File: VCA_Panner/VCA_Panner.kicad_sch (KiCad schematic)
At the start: 40 parts, among them J1 CV1, J2 Ch1_in, J3 Ch1_out, J4 CV2, J5 Ch2_in, J6 Ch2_out, SW1 SW_DPDT_x2, SW2 SW_DPDT_x2, U1 TL074, U2 AS3360, U3 TL072

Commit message: feitw bugfixes
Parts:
- removed C5: 47pF, symbol Device:C
- removed SW1, SW2: SW_DPDT_x2, symbol Switch:SW_DPDT_x2
- removed U3: TL072, 4ms_Package_SSOP:TSSOP-8_4.4x3mm_Pitch0.65mm, symbol PCM_4ms_IC:TL072
- added C10, C4, C8, C9: 0.1uF, Capacitor_SMD:C_0805_2012Metric_Pad1.18x1.45mm_HandSolder, symbol Device:C
- added C11: 470p, Capacitor_SMD:C_0805_2012Metric_Pad1.18x1.45mm_HandSolder, symbol Device:C
- added C12, C13: 47u, Capacitor_THT:CP_Radial_D4.0mm_P2.00mm, symbol Device:C_Polarized
- added D3, D4: 1N5819, Diode_THT:D_DO-41_SOD81_P2.54mm_Vertical_AnodeUp, symbol Diode:1N5819
- added J5: ~, mort_mix:Pins_2x05_2.54mm_TH_Europower_shrouded, symbol Connector_Generic:Conn_02x05_Odd_Even
- added R19, R21, R23, R7: 10k, Resistor_SMD:R_0805_2012Metric_Pad1.20x1.40mm_HandSolder, symbol Device:R
- added R20, R32, R36: 100k, Resistor_SMD:R_0805_2012Metric_Pad1.20x1.40mm_HandSolder, symbol Device:R
- added R22, R24, R8: 56k, Resistor_SMD:R_0805_2012Metric_Pad1.20x1.40mm_HandSolder, symbol Device:R
- added R25: 20k, Resistor_SMD:R_0805_2012Metric_Pad1.20x1.40mm_HandSolder, symbol Device:R
- added R26, R27: 47k, Resistor_SMD:R_0805_2012Metric_Pad1.20x1.40mm_HandSolder, symbol Device:R
- added R28: 330k, Resistor_SMD:R_0805_2012Metric_Pad1.20x1.40mm_HandSolder, symbol Device:R
- added R29, R33, R35: 51k, Resistor_SMD:R_0805_2012Metric_Pad1.20x1.40mm_HandSolder, symbol Device:R
- added R34: 1k, Resistor_SMD:R_0805_2012Metric_Pad1.20x1.40mm_HandSolder, symbol Device:R
- added R37, R38: 10, Resistor_SMD:R_0805_2012Metric_Pad1.20x1.40mm_HandSolder, symbol Device:R
- added R39, R40: 400k, Resistor_SMD:R_0805_2012Metric_Pad1.20x1.40mm_HandSolder, symbol Device:R
- added RV3, RV4: 100k_B, mort_mix:Potentiometer_Alpha_RD901F-40-00D_Single_Vertical_withhole, symbol Device:R_Potentiometer
- added U2, U3: TL074, Package_SO:SO-14_3.9x8.65mm_P1.27mm, symbol Amplifier_Operational:TL074
- C1, C2: value 47pF -> 0.1uF; footprint (none) -> Capacitor_SMD:C_0805_2012Metric_Pad1.18x1.45mm_HandSolder
- C3, C7: value 22pF -> 0.1uF; footprint (none) -> Capacitor_SMD:C_0805_2012Metric_Pad1.18x1.45mm_HandSolder
- C5: renamed from C4; value 10nF -> 4.7n; footprint (none) -> Capacitor_SMD:C_0805_2012Metric_Pad1.18x1.45mm_HandSolder
- C6: value 47pF -> 470p; footprint (none) -> Capacitor_SMD:C_0805_2012Metric_Pad1.18x1.45mm_HandSolder
- D1, D2: footprint (none) -> Diode_SMD:D_0805_2012Metric_Pad1.15x1.40mm_HandSolder
- J1: footprint (none) -> mort_mix:PJ398SM
- J2: renamed from J4; footprint (none) -> mort_mix:PJ398SM
- J3: renamed from J2; footprint (none) -> mort_mix:Jack_3.5mm_QingPu_WQP-PJ366ST_Vertical
- J4: renamed from J3; footprint (none) -> mort_mix:Jack_3.5mm_QingPu_WQP-PJ366ST_Vertical
- J6: renamed from J5; footprint (none) -> mort_mix:PJ398SM
- J7: renamed from J6; footprint (none) -> mort_mix:PJ398SM
- R1, R11, R2: footprint (none) -> Resistor_SMD:R_0805_2012Metric_Pad1.20x1.40mm_HandSolder
- R10, R18: value 100k -> 56k; footprint (none) -> Resistor_SMD:R_0805_2012Metric_Pad1.20x1.40mm_HandSolder
- R12: value 12k -> 47k; footprint (none) -> Resistor_SMD:R_0805_2012Metric_Pad1.20x1.40mm_HandSolder
- R13: value 100k -> 47k; footprint (none) -> Resistor_SMD:R_0805_2012Metric_Pad1.20x1.40mm_HandSolder
- R14: value 47k -> 330k; footprint (none) -> Resistor_SMD:R_0805_2012Metric_Pad1.20x1.40mm_HandSolder
- R15: value 1k -> 100k; footprint (none) -> Resistor_SMD:R_0805_2012Metric_Pad1.20x1.40mm_HandSolder
- R16, R6: value 47k -> 100k; footprint (none) -> Resistor_SMD:R_0805_2012Metric_Pad1.20x1.40mm_HandSolder
- R17, R5, R9: value 100k -> 10k; footprint (none) -> Resistor_SMD:R_0805_2012Metric_Pad1.20x1.40mm_HandSolder
- R3: value 20k -> 10k; footprint (none) -> Resistor_SMD:R_0805_2012Metric_Pad1.20x1.40mm_HandSolder
- R30: renamed from R7; footprint (none) -> Resistor_SMD:R_0805_2012Metric_Pad1.20x1.40mm_HandSolder
- R31: renamed from R8; value 47k -> 51k; footprint (none) -> Resistor_SMD:R_0805_2012Metric_Pad1.20x1.40mm_HandSolder
- R4: value 12k -> 56k; footprint (none) -> Resistor_SMD:R_0805_2012Metric_Pad1.20x1.40mm_HandSolder
- RV1, RV2: value 10k -> 100k_B; footprint (none) -> mort_mix:Potentiometer_Alpha_RD901F-40-00D_Single_Vertical_withhole
- U1: footprint (none) -> Package_SO:SO-14_3.9x8.65mm_P1.27mm
- U5: renamed from U2; footprint (none) -> Package_SO:SOIC-16_3.9x9.9mm_P1.27mm
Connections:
- net CV_to_ch1 is gone; now on net CV2: J2.T
- net CV_to_ch2 is gone; now on an unnamed net: D2.2 (A)
- net audio_to_ch1 is gone; now on net audio_from_ch2: J7.TN
- net +12V: now also C1.1, C2.1, C3.1, U1.4 (V+), C13.1, C4.2, R37.1, R39.2, R40.2, U2.4 (V+), U3.4 (V+)
- net -12V: now also C7.2, U1.11 (V-), C10.2, C12.2, C8.2, C9.2, R38.2, U2.11 (V-), U3.11 (V-); no longer R12.1, R4.1
- net GND: now also C1.2, C2.2, C3.2, C7.1, R13.2, C10.1, C12.1, C13.2, C4.1, C8.1, C9.1, J5.3 (Pin_3), J5.4 (Pin_4), J5.5 (Pin_5), J5.6 (Pin_6), J5.7 (Pin_7), J5.8 (Pin_8), R27.2, R35.1, RV3.1, RV4.1, U2.10 (+), U2.3 (+), U3.12 (+), U3.5 (+); no longer R16.1, U1.10 (+), U1.3 (+)
- net at R31.2, U5.2 (IO1): now also U2.6 (-); no longer C3.1, R5.1
- net CV1: now reaches D1.1 (K)
- net CV1: now also R12.1, R6.2, RV1.3
- net at R12.2: now also R13.1, RV1.2, U1.3 (+); no longer RV2.3
- net at R18.2: now also R23.1, U3.13 (-)
- net at R14.1: now also RV2.3; no longer J6.T
- net at R6.1: now also R1.2, U1.2 (-); no longer J3.R
- net audio1_to_vca1: now reaches U5.6 (II1)
- net audio1_to_vca1: now also R29.2; no longer R6.2
- net at R11.2: now also R5.1, U2.1; no longer U5.10 (VC2)
- net at R9.1: now also R4.2, U1.13 (-); no longer U1.14
- net at R3.2: now also U1.9 (-), R8.1; no longer U5.5 (VC1)
- net at R17.2: now also R22.1, U3.9 (-)
- net at R15.2: now also R20.1, U3.2 (-); no longer J7.T
- net at R14.2: now also R40.1; no longer U5.9 (II2)
- net CV_from_ch1: no longer names the net of J2.TN
- net CV_from_ch2 renamed CV2
- net CV2: now also R20.2, R26.1, RV3.3
- new net: R3.1, R9.2, U1.8
- new net: RV2.2, U1.10 (+)
- new net: R15.1, R21.2, U3.1
- new net: R26.2, R27.1, RV3.2, U3.3 (+)
- new net: R18.1, R24.2, U3.14
- new net: R10.1, R5.2, U2.2 (-)
- new net: R10.2, R4.1, U1.14
- new net: D4.2 (A), R38.1
- new net: R16.1, R22.2, U3.7
- new net: R16.2, R21.1, U3.6 (-)
- new net: C11.2, R34.1, R36.1, U2.14
- new net: C11.1, R36.2, U2.12 (+)
- new net: R19.2, R24.1, U2.9 (-)
- new net: D3.1 (K), R37.2
- new net: C6.1, R32.2, U2.5 (+)
- new net: C6.2, R30.1, R32.1, U2.7
- new net: R28.1, RV4.3
- new net: R28.2, R39.1
- new net: D3.2 (A), J5.10 (Pin_10), J5.9 (Pin_9)
- new net: J7.T, R34.2
- new net: R1.1, R7.2, U1.1
- new net: R17.1, R23.2, U3.8
- new net: R35.2, U2.13 (-), U5.13 (IO2)
- new net: RV4.2, U3.10 (+)
- new net: J6.T, R33.2
- new net: R2.1, R8.2, U1.7
- new net: R19.1, R25.2, U2.8
- new net: J3.R, R29.1
- new net: D4.1 (K), J5.1 (Pin_1), J5.2 (Pin_2)
- new net: R2.2, R7.1, U1.6 (-)
- new net audio2_to_vca2: R33.1, U5.9 (II2)
- new net cv1_to_vca1: R11.1, U5.5 (VC1)
- new net cv2_to_vca2: R25.1, U5.10 (VC2)
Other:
- removed sheet Untitled Sheet
- company: (none) -> Clandestine Circutry
- title: (none) -> VCA_Panner
- moved on the sheet: C5, D1, D2, J1, J2, J3, J4, J6, J7, R30, R31, U5A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

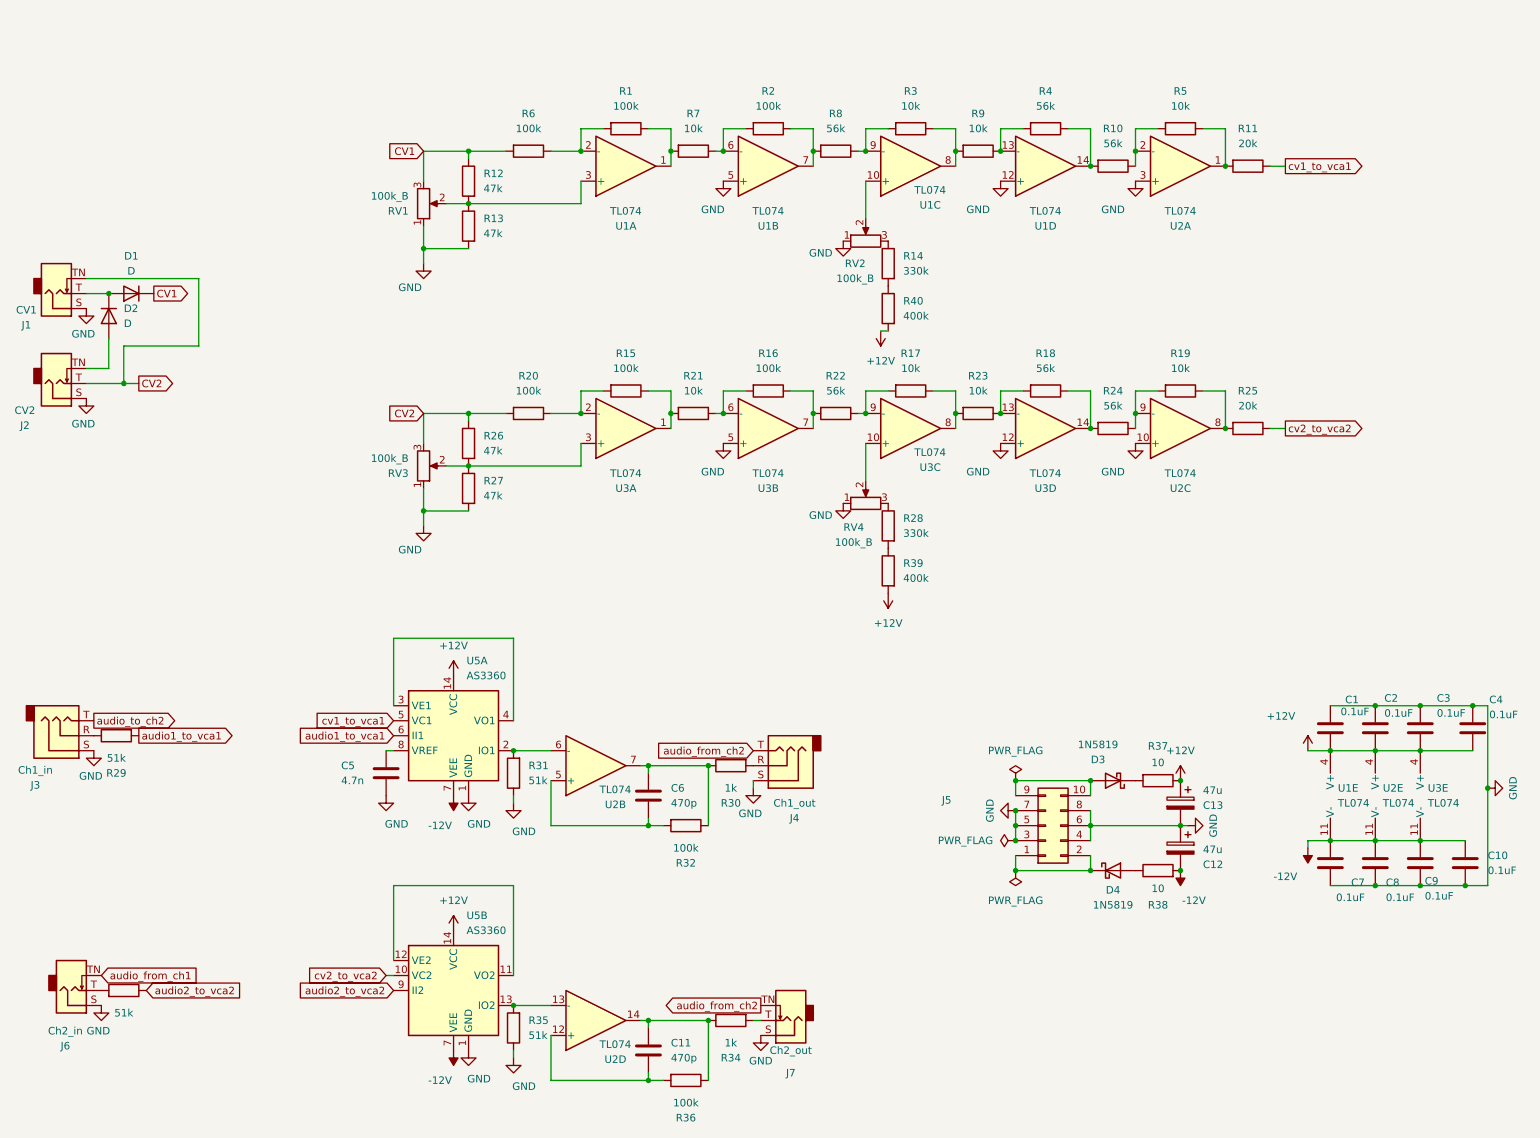
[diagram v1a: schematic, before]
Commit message: vca_panner led added, routing started
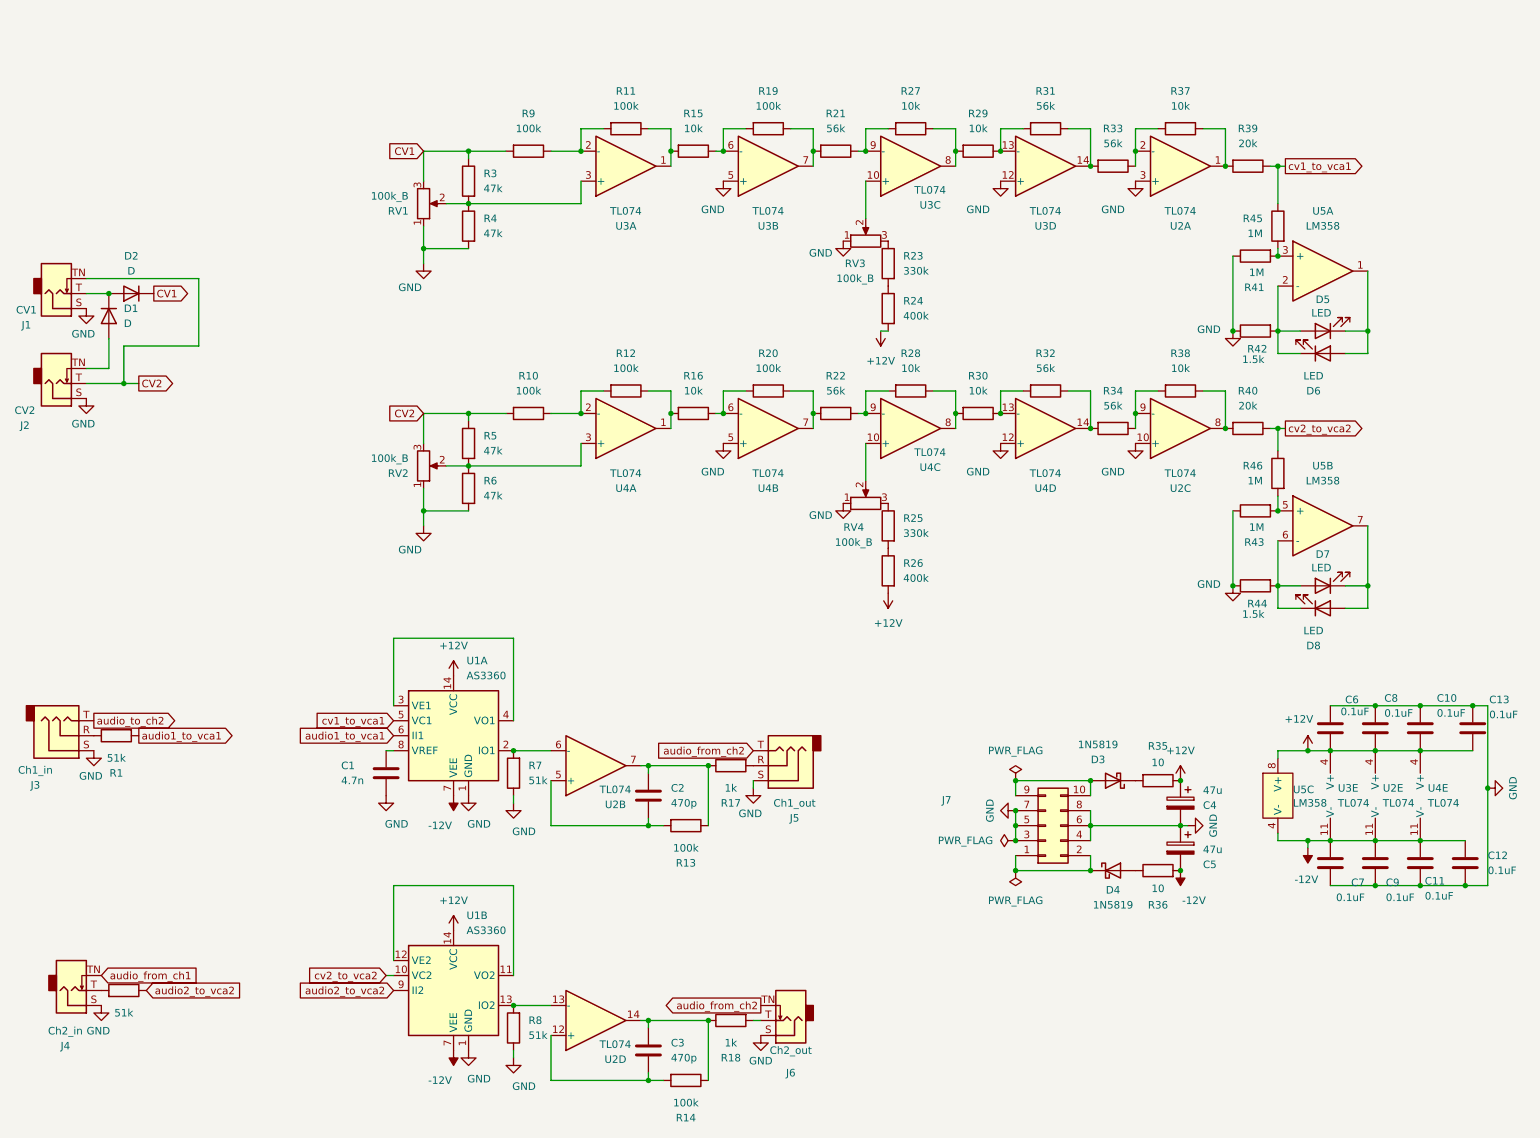
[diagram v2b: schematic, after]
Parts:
- added D5, D6, D7, D8: LED, LED_THT:LED_D3.0mm, symbol Device:LED
- added R41, R43, R45, R46: 1M, Resistor_SMD:R_0805_2012Metric_Pad1.20x1.40mm_HandSolder, symbol Device:R
- added R42, R44: 1.5k, Resistor_SMD:R_0805_2012Metric_Pad1.20x1.40mm_HandSolder, symbol Device:R
- added U5: LM358, Package_SO:SO-8_3.9x4.9mm_P1.27mm, symbol PCM_4ms_IC:LM358
- renumbered C5 to C1, C3 to C10, C9 to C11, C10 to C12, C4 to C13, C6 to C2, C11 to C3, C13 to C4, C12 to C5, C1 to C6, C2 to C8, C8 to C9, D2 to D1, D1 to D2, J6 to J4, J4 to J5, J7 to J6, J5 to J7, R29 to R1, R20 to R10, R1 to R11, R15 to R12, R32 to R13, R36 to R14, R7 to R15, R21 to R16, R30 to R17, R34 to R18, R2 to R19, R33 to R2, R16 to R20, R8 to R21, R14 to R23, R40 to R24, R28 to R25, R39 to R26, R3 to R27, R17 to R28, R9 to R29, R12 to R3, R23 to R30, R4 to R31, R18 to R32, R10 to R33, R24 to R34, R37 to R35, R38 to R36, R5 to R37, R19 to R38, R11 to R39, R13 to R4, R25 to R40, R26 to R5, R27 to R6, R31 to R7, R35 to R8, R6 to R9, RV3 to RV2, RV2 to RV3, U5 to U1, U1 to U3, U3 to U4
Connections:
- net +12V: now also U5.8 (V+)
- net -12V: now also U5.4 (V-)
- net GND: now also R41.1, R42.1, R43.1, R44.1
- net cv1_to_vca1: now also R45.1
- net cv2_to_vca2: now also R46.1
- new net: D7.1 (K), D8.2 (A), U5.7
- new net: D7.2 (A), D8.1 (K), R44.2, U5.6 (-)
- new net: R43.2, R46.2, U5.5 (+)
- new net: D5.1 (K), D6.2 (A), U5.1
- new net: D5.2 (A), D6.1 (K), R42.2, U5.2 (-)
- new net: R41.2, R45.2, U5.3 (+)

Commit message: pcb done, next panel
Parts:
- removed D5, D7: LED, LED_THT:LED_D3.0mm, symbol Device:LED
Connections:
- net audio_from_ch1 is gone; now on net audio_to_ch2: J4.TN
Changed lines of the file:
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@@
 	)
 	(junction
-		(at 243.84 106.68)
-		(diameter 0)
-		(color 0 0 0 0)
-	)
-	(junction
 		(at 212.09 154.94)
 		(diameter 0)
@@
 	)
 	(junction
-		(at 243.84 63.5)
-		(diameter 0)
-		(color 0 0 0 0)
-	)
-	(junction
 		(at 134.62 33.02)
 		(diameter 0)
@@
 	(wire
 		(pts
-			(xy 232.41 63.5) (xy 228.6 63.5)
-		)
-		(stroke
-			(width 0)
-			(type default)
-		)
-	)
-	(wire
-		(pts
 			(xy 121.92 137.16) (xy 121.92 138.43)
 		)
@@
 	(wire
 		(pts
-			(xy 243.84 63.5) (xy 243.84 67.31)
+			(xy 243.84 53.34) (xy 243.84 67.31)
 		)
 		(stroke
@@
 	(wire
 		(pts
-			(xy 243.84 106.68) (xy 243.84 110.49)
-		)
-		(stroke
-			(width 0)
-			(type default)
-		)
-	)
-	(wire
-		(pts
 			(xy 232.41 67.31) (xy 228.6 67.31)
 		)
@@
 	(wire
 		(pts
-			(xy 232.41 106.68) (xy 228.6 106.68)
-		)
-		(stroke
-			(width 0)
-			(type default)
-		)
-	)
-	(wire
-		(pts
 			(xy 173.99 29.21) (xy 170.18 29.21)
 		)
@@
 	(wire
 		(pts
-			(xy 240.03 63.5) (xy 243.84 63.5)
-		)
-		(stroke
-			(width 0)
-			(type default)
-		)
-	)
-	(wire
-		(pts
 			(xy 193.04 73.66) (xy 196.85 73.66)
 		)
@@
 	(wire
 		(pts
-			(xy 243.84 96.52) (xy 243.84 106.68)
+			(xy 243.84 96.52) (xy 243.84 110.49)
 		)
 		(stroke
@@
 	(wire
 		(pts
-			(xy 240.03 106.68) (xy 243.84 106.68)
-		)
-		(stroke
-			(width 0)
-			(type default)
-		)
-	)
-	(wire
-		(pts
 			(xy 91.44 41.91) (xy 110.49 41.91)
 		)
@@
 	(wire
 		(pts
-			(xy 243.84 53.34) (xy 243.84 63.5)
-		)
-		(stroke
-			(width 0)
-			(type default)
-		)
-	)
-	(wire
-		(pts
 			(xy 228.6 80.01) (xy 228.6 83.82)
 		)
@@
 		)
 	)
-	(global_label "audio_from_ch1"
+	(global_label "audio_to_ch2"
 		(shape input)
 		(at 29.21 172.72 0)
@@
 		)
 		(property "Intersheetrefs" "${INTERSHEET_REFS}"
-			(at 47.1325 172.72 0)
+			(at 44.653 172.72 0)
 			(effects
 				(font
@@
 	)
 	(symbol
-		(lib_id "Device:LED")
-		(at 236.22 106.68 180)
-		(unit 1)
-		(exclude_from_sim no)
-		(in_bom yes)
-		(on_board yes)
-		(dnp no)
-		(property "Reference" "D7"
-			(at 236.22 101.346 0)
-			(effects
-				(font
-					(size 1.27 1.27)
-				)
-			)
-		)
-		(property "Value" "LED"
-			(at 235.966 103.632 0)
-			(effects
-				(font
-					(size 1.27 1.27)
-				)
-			)
-		)
-		(property "Footprint" "LED_THT:LED_D3.0mm"
-			(at 236.22 106.68 0)
-			(effects
-				(font
-					(size 1.27 1.27)
-				)
-				(hide yes)
-			)
-		)
-		(property "Datasheet" "~"
-			(at 236.22 106.68 0)
-			(effects
-				(font
-					(size 1.27 1.27)
-				)
-				(hide yes)
-			)
-		)
-		(property "Description" "Light emitting diode"
-			(at 236.22 106.68 0)
-			(effects
-				(font
-					(size 1.27 1.27)
-				)
-				(hide yes)
-			)
-		)
-		(pin "1"
-		)
-		(pin "2"
-		)
-		(instances
-			(project "VCA_Panner"
-				(path "/416439c0-fe9f-449c-a999-c0ea4c6cd459"
-					(reference "D7")
-					(unit 1)
-				)
-			)
-		)
-	)
-	(symbol
 		(lib_id "Device:R_Potentiometer")
 		(at 83.82 41.91 0)
@@
 					(unit 1)
 				)
-			)
-		)
-	)
-	(symbol
-		(lib_id "Device:LED")
-		(at 236.22 63.5 180)
-		(unit 1)
-		(exclude_from_sim no)
-		(in_bom yes)
-		(on_board yes)
-		(dnp no)
-		(property "Reference" "D5"
-			(at 236.22 58.166 0)
-			(effects
-				(font
-					(size 1.27 1.27)
-				)
-			)
-		)
-		(property "Value" "LED"
-			(at 235.966 60.452 0)
-			(effects
-				(font
-					(size 1.27 1.27)
-				)
-			)
-		)
-		(property "Footprint" "LED_THT:LED_D3.0mm"
-			(at 236.22 63.5 0)
-			(effects
-				(font
-					(size 1.27 1.27)
-				)
-				(hide yes)
-			)
-		)
-		(property "Datasheet" "~"
-			(at 236.22 63.5 0)
-			(effects
-				(font
-					(size 1.27 1.27)
-				)
-				(hide yes)
-			)
-		)
-		(property "Description" "Light emitting diode"
-			(at 236.22 63.5 0)
-			(effects
-				(font
-					(size 1.27 1.27)
-				)
-				(hide yes)
-			)
-		)
-		(pin "1"
-		)
-		(pin "2"
-		)
-		(instances
-			(project "VCA_Panner"
-				(path "/416439c0-fe9f-449c-a999-c0ea4c6cd459"
-					(reference "D5")
-					(unit 1)
-				)
